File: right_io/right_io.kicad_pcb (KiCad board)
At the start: 8 copper layers, 58 x 185 mm, 163 parts, among them J11 USB-C dual-role data/PD port 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, J12 USB-C source-only data port J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, J30 External HDMI-A from TCP0, J500 JXD1-1022NL recessed 1GbE RJ45, Q2002 2N7002K DFP USB2 enable inver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, Q50 BSS138 HDMI bias gate, U1760 TPS2553DDBVR 1.3A USB branch, U1761 TPS25810RVCR Type-C DFP contr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, U1763 TPD1S514-1YZR 5.9V VBUS OVP, U1765 TPD4E05U06 USB2/CC ESD, U2011 TPD4S201 CC and USB2 short-to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, U2012 CAT24C256 32KB private TPS257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, U2013 TS3USB30E DFP-qualified USB2 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, U2014 SN74LVC2G07 partial-power-dow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, U2015 TVS2200 22V USB VBUS surge cl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, U2016 SN74LVC1G08 DFP and attached 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, U42 TPS25751AD USB-PD DRP control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, U50 TPD13S523PWR HDMI control ESD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, U500 RTL8111H-CG-RH PCIe Gigabit E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, U501 D3V3XA4B10LP-7 four-channel 0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, U502 D3V3XA4B10LP-7 four-channel 0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, U51 PCA9306DCTR HDMI DDC level tr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, U53 SN74LVC1G17DBVR HDMI HPD buff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, U54 TPS22975NDSGR host-active SYS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, U55 TPS22975NDSGR host-active SYS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, U721 TPS26630RGER PD2 default-off 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, Y500 ECS-250-8-33-AGN-TR 25MHz 8pF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

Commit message: Board split Phase 4a: FPC connectors wired through the four split schematics
Connector symbols and sheets now exist in every project and the boundary
nets are pinned through them (same conductor order on both ends, verified
netlist-by-netlist):
  - gen/fpc_contract.py: authoritative FPC-1/2/3 pin maps + center-side
    renames (single source of truth for schematics, board pad nets, cable
    spec, and gate contracts)
  - gen/Conn_01x100_FFC_MP.kicad_sym (derived from the 30-pin pattern)
  - center: real fpc1_left/fpc2_right/fpc3_bms sheets wired to host pins
  - left_io/right_io: left_fpc/right_fpc connector sheets; bms carries
    FPC106 inline
  - connector refs FPC101..FPC106 (valid designators; FPC1_L-style refs
    broke KiCad annotation)
  - pack-rail naming reconciled: center gauge divider BAT_PROT_VIN ->
    PACK_POS_FUSED (same node as the BMS LTC4368 output); BMS ground
    /GND -> GND (pack negative is the system ground)

Boards: daughterboards re-synced from their connector-bearing schematics;
center connectors placed and their pad nets assigned text-side ((net
"name") convention).  Connector pads verified against every other
footprint (0 overlaps) and DRC shows 0 shorts on all four boards (center
16 pre-existing, down from 17).

Fixed two latent generator bugs exposed by the wiring:
  - resolve_connectors used naive +R rotation, placing Phase 3 connectors
    against mirrored phantom positions
  - pad half-extents were computed as footprint_rot+pad_rot, but KiCad
    saves pads with world orientation (FH12-100S pins are 1.3mm wide);
    both verified empirically against pcbnew, plus a connector-nudge pass
    for parts sandwiched between the connector body and pin columns

Gate: SCHEMATIC RELEASE CHECK: PASS (FPC pin contracts added per project;
closure audits 0 FAIL).  Routing remains manual (Phase 4b).
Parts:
- removed FPC2_R: FH12-100S-0.5SH_1x100-1MP_P0.50mm_Horizontal, ducktop2:FH12-100S-0.5SH_1x100-1MP_P0.50mm_Horizontal
- added FPC104: FH12-100S-0.5SH (FPC-2), ducktop2:FH12-100S-0.5SH_1x100-1MP_P0.50mm_Horizontal, F.Cu at (302.7, 92.5)

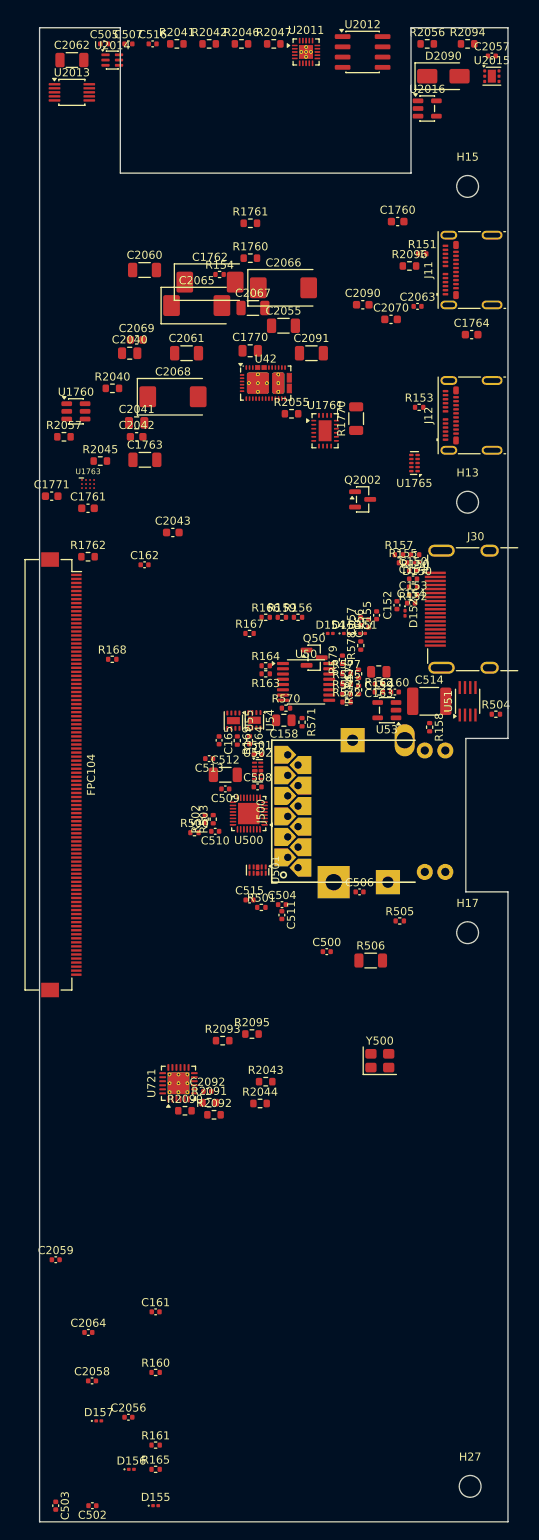
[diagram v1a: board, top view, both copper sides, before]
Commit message: Phase 4 deep audit: FH41-68S connectors, placement hygiene, one-shot fixes
Found and fixed four board-killers in the pre-fab audit:

1. Fictional connector: the Hirose FH12 series stops at 60 positions, so
   the 100-pin FH12-100S used for FPC-1/FPC-2 does not exist.  Replaced
   with the FH41-68S-0.5SH(05) (shielded-FFC, 68 positions; FPC-1 uses
   pins 1-53, FPC-2 pins 1-61):
   - new footprint derived from KiCad's FH41-30S (68 signal pads, MP at
     +/-18, 14 SH solder-holds, 38mm body) with SH pads tied to GND
   - new 68-pin symbol (Conn_01x68_FFC_MP), pin maps trimmed to 68
   - fictional FH12-100S footprint/symbol/script removed
   - cable spec updated (68-pin shielded FFC, one type for both)

2. Connector courtyard conflicts: parts sat under connector bodies
   (pads cleared, bodies collided).  Placement now enforces courtyard
   clearance against the connector body; the resolver scans with
   courtyard checks; a double-shift bug that hid re-placed parts' true
   positions was fixed.

3. FPC-3 orientation: the FH12's FPC enters from the +y side; both FPC-3
   connectors faced away from the seam.  FPC105 -> (123.5, 6.5) rot 180,
   FPC106 -> (30, 54) rot 0 so the cable exits the center bottom edge
   and enters the BMS top edge.

4. Original-layout defects: 16 genuine pad-pad shorts (inductor pads
   swallowing caps, passives on each other, parts on mounting holes) and
   23 parts inside the hinge cutouts (physically off the board) are all
   moved to legal spots; zones refilled against the final placement.

New post-build hygiene sweep (fix_board_hygiene.py) uses the final board
text as the geometry oracle, converges to a clean state, and reports
residuals instead of dropping them.

Final DRC: 0 shorts / 0 clearance / 0 hole violations on all four boards
(bms fully clean).  Remaining: courtyard touches around the Mu socket and
M.2 slot (design-inherent moat), chassis-edge copper, zone islands, silk
cosmetics, and unrouted nets (Phase 4b).  Gate: SCHEMATIC R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
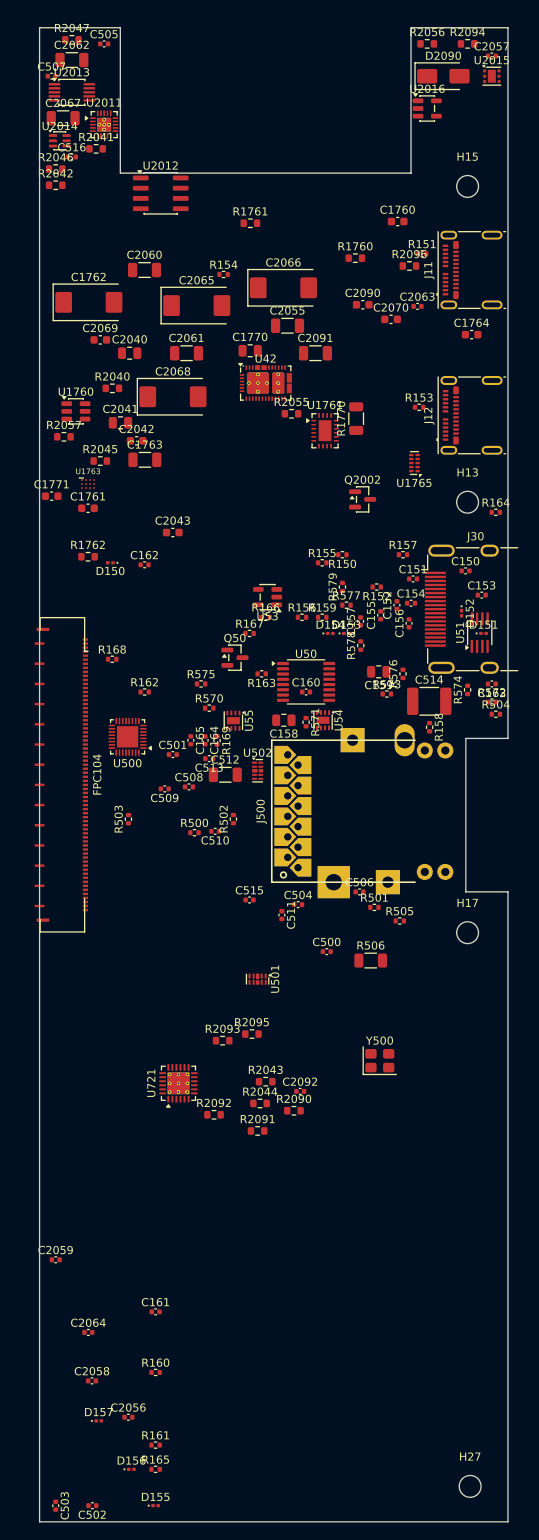
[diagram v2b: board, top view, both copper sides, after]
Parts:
- FPC104: value FH12-100S-0.5SH (FPC-2) -> FH41-68S-0.5SH (FPC-2); footprint ducktop2:FH12-100S-0.5SH_1x100-1MP_P0.50mm_Horizontal -> ducktop2:Hirose_FH41-68S-0.5SH_1x68_1MP_1SH_P0.5mm_Horizontal
- moved D150 38.0 mm to (308.8, 66.2)
- moved R164 34.3 mm to (356.5, 60.0)
- moved C2067 33.2 mm to (302.9, 11.2)
- moved U2012 30.5 mm to (315.0, 20.5)
- moved R162 29.0 mm to (313.0, 82.2)
- moved R2046 27.7 mm to (302.0, 17.5)
- moved U2011 26.6 mm to (308.0, 12.0)
- moved R2042 25.8 mm to (302.0, 19.5)
- moved R2047 25.0 mm to (304.0, 1.50)
- moved U53 20.4 mm to (328.2, 70.5)
- moved R572 18.0 mm to (356.0, 83.5)
- moved R575 18.0 mm to (320.0, 81.2)
- moved U500 17.8 mm to (310.9, 87.8)
- moved C516 17.2 mm to (304.0, 16.0)
- moved R2041 16.4 mm to (307.0, 15.0)
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
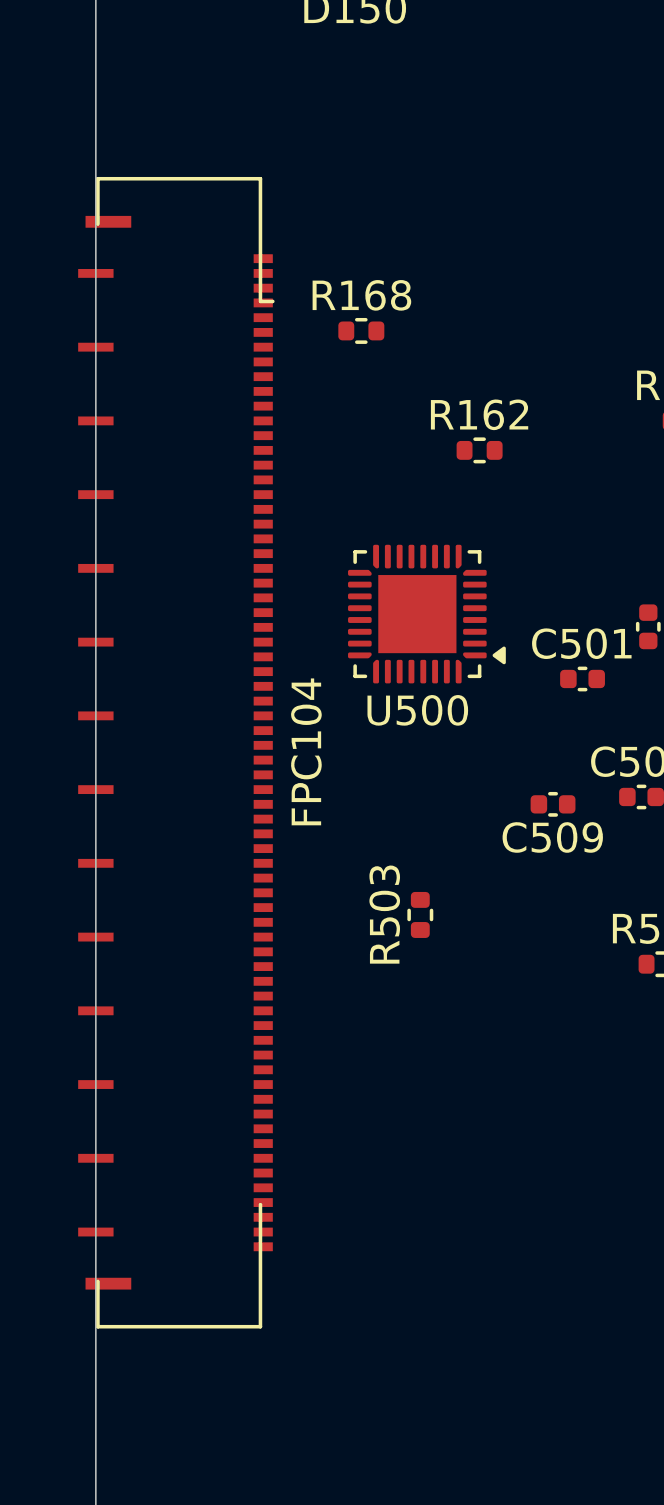
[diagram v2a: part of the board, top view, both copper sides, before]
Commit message: Deep audit completion: FPC anchors over cut lines, FPC106 rotation, pro rules
Follow-up fixes found while closing out the audit:
- FPC102/FPC104 FH41 MP tabs poked across the internal cut lines (pads
  physically off their boards): anchors moved to (73.5, 92.5) and
  (303.6, 92.5); all four boards now report 0 boundary crossings.
- FPC106 had reverted to the seam-away rotation; restored to (30, 54)
  rot 0 (cable enters from the BMS top edge).
- The MCP board sync clobbers the daughterboard .kicad_pro design rules;
  inherit_netclasses now restores them (min_through_hole 0.2, min_track
  0.09, min_clearance 0.09) so the DRC is honest about the 0.2mm drills.
- ERC triaged on all four projects: remaining items are cross-board
  power nets (driver on the other side of an FPC), power-flag artifacts,
  or intentional NCs -- no genuine errors.
- FH41-68S-0.5SH confirmed orderable (DigiKey/Mouser in stock).
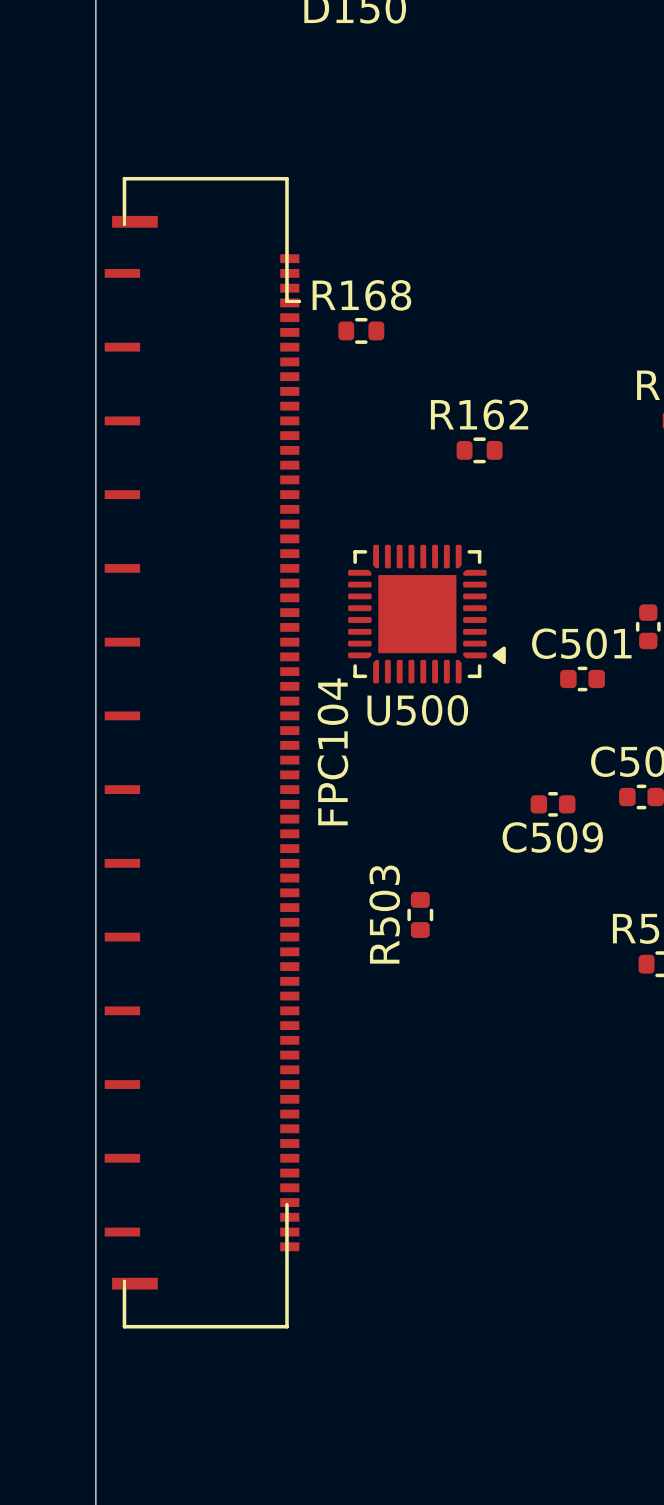
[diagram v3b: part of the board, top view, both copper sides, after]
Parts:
- moved FPC104 0.90 mm to (303.6, 92.5)
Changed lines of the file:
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@@
 	(footprint "ducktop2:Hirose_FH41-68S-0.5SH_1x68_1MP_1SH_P0.5mm_Horizontal"
 		(layer "F.Cu")
-		(at 302.7 92.5 -90)
+		(at 303.6 92.5 -90)
 		(descr "Hirose FH41, FFC/FPC connector, FH41-68S-0.5SH, 68 Pins per row (board split FPC-1/FPC-2; derived from the KiCad FH41-30S)")
 		(tags "connector Hirose FH41 horizontal")
